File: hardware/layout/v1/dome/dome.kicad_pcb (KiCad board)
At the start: 4 copper layers, 13.6 x 13.6 mm, 7 parts, among them J1 CROWN_RISER, U1 LTR-390UV-01, U2 TSL25911FN, U3 GUVB-C31SM

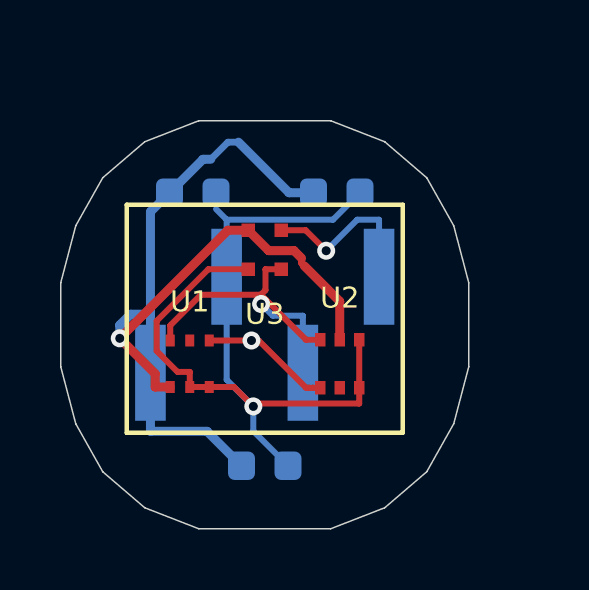
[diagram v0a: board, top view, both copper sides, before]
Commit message: Update dome PCB to Genicom GUVB-C21SD/GUVA-C22SD photodiodes with TLV9062 transimpedance and ADS1115 ADC, increase diameter to Ø 15.6 mm
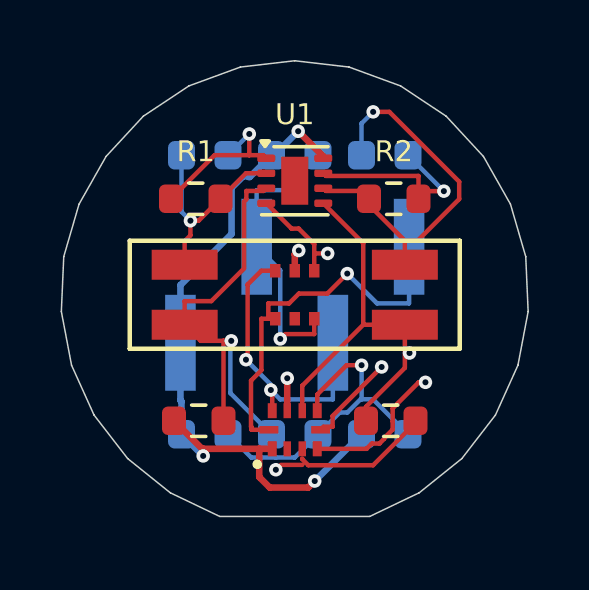
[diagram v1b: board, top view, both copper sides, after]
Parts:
- added C4: 10n 50V, Capacitor_SMD:C_0603_1608Metric, B.Cu at (4.80, -12.4)
- added C5: 22n 50V, Capacitor_SMD:C_0603_1608Metric, B.Cu at (10.8, -12.4)
- added C6: 1u 50V, Capacitor_SMD:C_0603_1608Metric, B.Cu at (7.80, -3.15)
- added D1: GUVB-C21SD, gateway_fp:Genicom_COB2418, F.Cu at (4.13, -7.80)
- added D2: GUVA-C22SD, gateway_fp:Genicom_COB2418, F.Cu at (11.5, -7.80)
- added R1: 10M, Resistor_SMD:R_0603_1608Metric, F.Cu at (4.50, -11.0)
- added R2: 4M7, Resistor_SMD:R_0603_1608Metric, F.Cu at (11.1, -11.0)
- added R3: 100k, Resistor_SMD:R_0603_1608Metric, F.Cu at (4.60, -3.60)
- added R4: 10k, Resistor_SMD:R_0603_1608Metric, F.Cu at (11.0, -3.60)
- C3: value 1u 50V -> 100n 50V
- U1: value LTR-390UV-01 -> TLV9062IDSGR; footprint gateway_fp:LiteOn_LTR-390UV-01 -> Package_SON:Texas_DSG0008A_WSON-8-1EP_2x2mm_P0.5mm_EP0.9x1.6mm
- U3: value GUVB-C31SM -> ADS1115IRUGR; footprint gateway_fp:GenUV_GUVB-C31SM -> gateway_fp:TI_ADS1115_X2QFN-10
- moved C1 10.3 mm to (10.8, -3.15)
- moved U1 7.03 mm to (7.80, -11.6)
- moved U3 6.08 mm to (7.80, -3.30)
- moved U2 2.75 mm to (7.80, -7.80)
- moved C3 2.26 mm to (4.80, -3.15)
- moved C2 1.88 mm to (7.80, -12.4)
- moved J1 1.41 mm to (7.80, -7.80)
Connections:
- U1 pad 1: +3V3 -> UVB_OUT
- U1 pad 2: GND -> UVB_IN
- U1 pad 3: GND -> UV_VB
- U1 pad 4: I2C_SCL -> GND
- U1 pad 5: (no net) -> UV_VB
- U1 pad 6: I2C_SDA -> UVA_IN
- U3 pad 1: GND -> +3V3
- U3 pad 2: I2C_SDA -> (no net)
- U3 pad 3: I2C_SCL -> GND
- U3 pad 4: +3V3 -> UVB_OUT
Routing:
- net UV_VB: track 0.00 -> 34.9 mm, vias 0 -> 2
- net UVB_OUT: track 0.00 -> 26.0 mm, vias 0 -> 2
- net UVA_OUT: track 0.00 -> 17.1 mm, vias 0 -> 2
- net UVA_IN: track 0.00 -> 12.8 mm, vias 0 -> 1
- net UVB_IN: track 0.00 -> 7.04 mm, vias 0 -> 1
- net I2C_SDA: track 11.7 -> 9.79 mm, vias 1 -> 2
- net I2C_SCL: track 14.2 -> 12.8 mm, vias 2 -> 1
- net +3V3: track 33.3 -> 32.9 mm, vias 1 -> 5
- net GND: track 29.0 -> 29.1 mm, vias 1 -> 4
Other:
- board size 13.6 x 13.6 mm -> 15.6 x 15.2 mm

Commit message: Update dome PCB layout with manual reference and label placement, add Stock_Optional field for LTR-390UV-01 sensor to allow JLC assembly when in stock without failing release on shortage
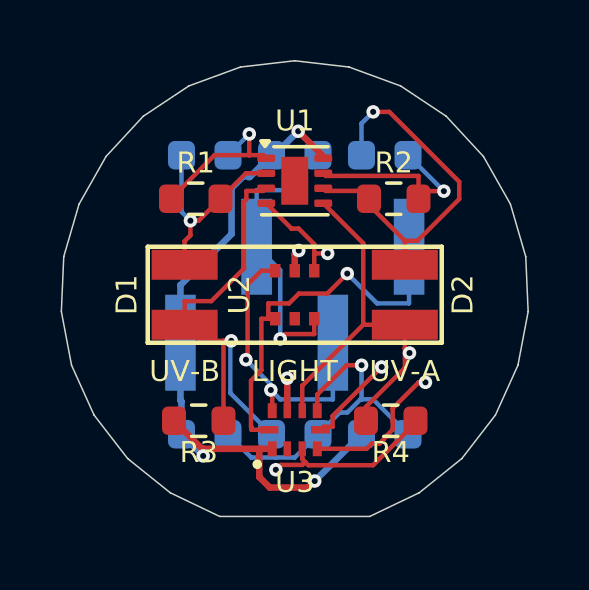
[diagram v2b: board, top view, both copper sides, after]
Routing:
- net GND: track 29.1 -> 30.1 mm
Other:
- board text added: "LIGHT"
- board text added: "UV-A"
- board text added: "UV-B"
